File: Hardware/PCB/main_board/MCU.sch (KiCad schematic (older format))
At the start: 2 parts, among them J1 SWD, U2 NUCLEO-F446RE

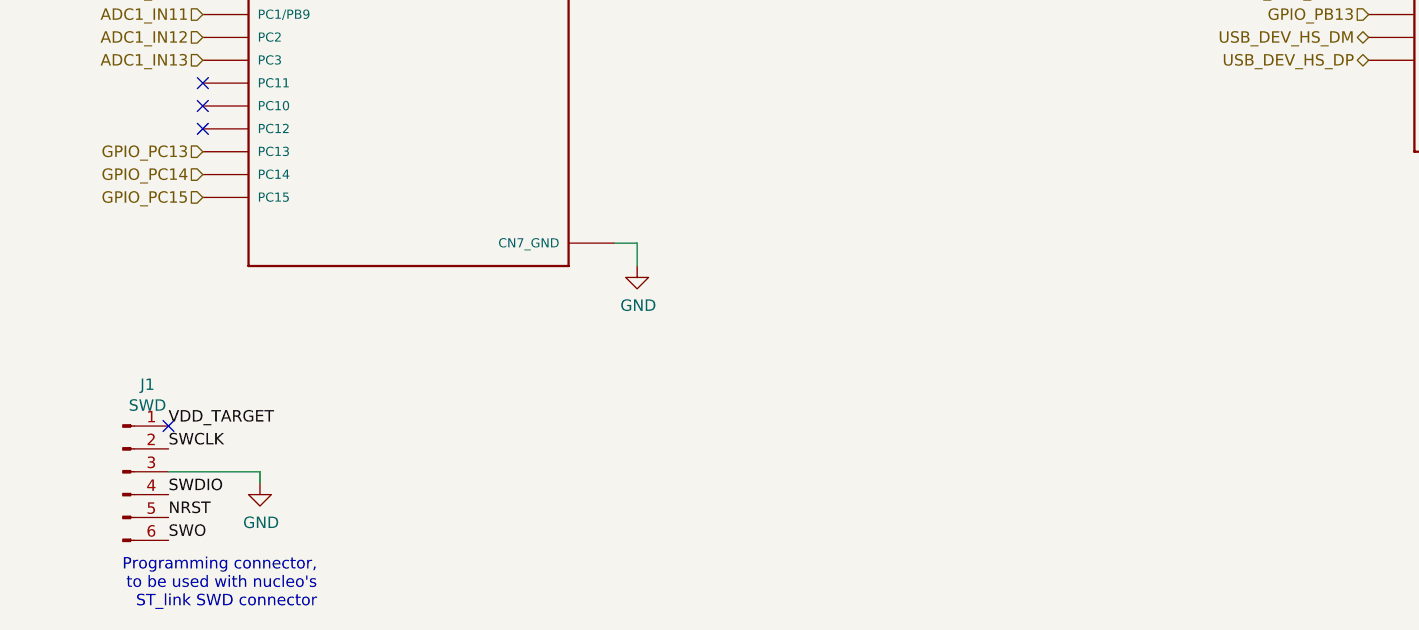
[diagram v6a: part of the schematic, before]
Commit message: Add test points headers
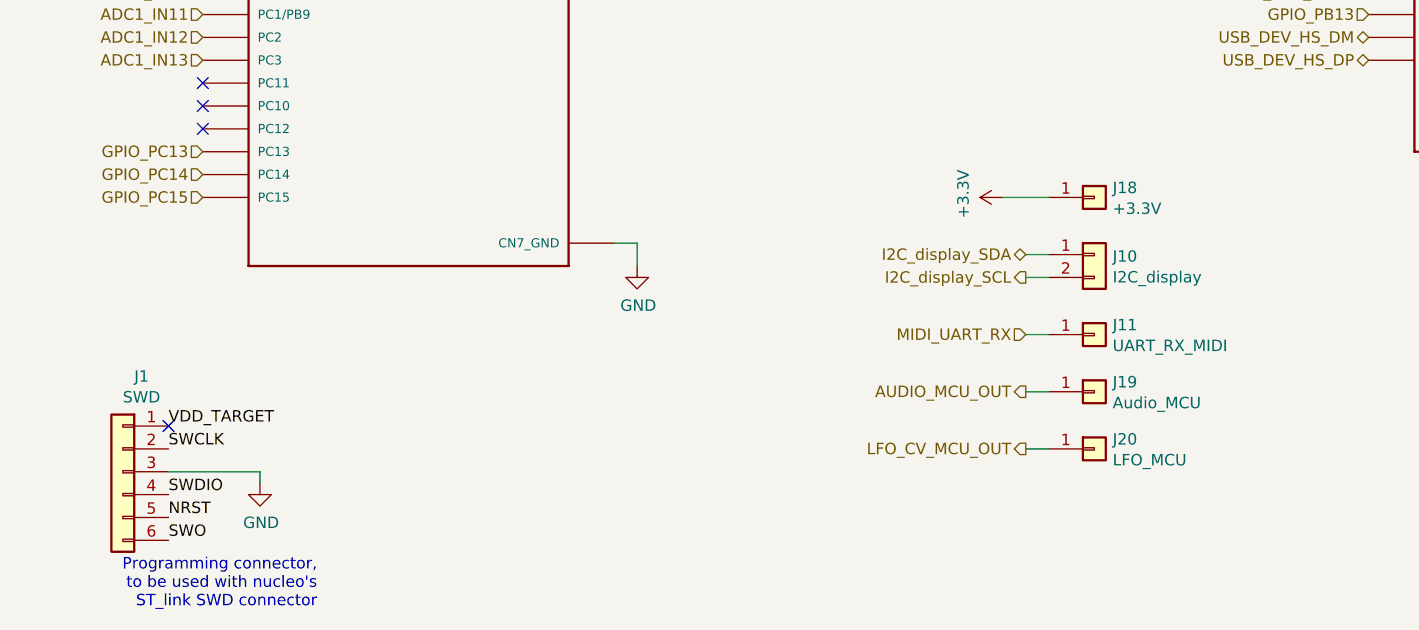
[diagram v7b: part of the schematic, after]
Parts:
- removed J1: SWD, Connector_PinHeader_2.54mm:PinHeader_1x06_P2.54mm_Vertical, symbol Connector:Conn_01x06_Male
- added J1: SWD, Connector_PinHeader_2.54mm:PinHeader_1x06_P2.54mm_Vertical, symbol Connector_Generic:Conn_01x06
- added J10: I2C_display, Connector_PinHeader_2.54mm:PinHeader_1x02_P2.54mm_Vertical, symbol Connector_Generic:Conn_01x02
- added J11: UART_RX_MIDI, Connector_PinHeader_2.54mm:PinHeader_1x01_P2.54mm_Vertical, symbol Connector_Generic:Conn_01x01
- added J18: +3.3V, Connector_PinHeader_2.54mm:PinHeader_1x01_P2.54mm_Vertical, symbol Connector_Generic:Conn_01x01
- added J19: Audio_MCU, Connector_PinHeader_2.54mm:PinHeader_1x01_P2.54mm_Vertical, symbol Connector_Generic:Conn_01x01
- added J20: LFO_MCU, Connector_PinHeader_2.54mm:PinHeader_1x01_P2.54mm_Vertical, symbol Connector_Generic:Conn_01x01
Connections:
- net +3V3: now also J18.1 (Pin_1)
- net AUDIO_MCU_OUT: now also J19.1 (Pin_1)
- net GND: now also J1.3 (Pin_3)
- net I2C_display_SCL: now also J10.2 (Pin_2)
- net I2C_display_SDA: now also J10.1 (Pin_1)
- net LFO_CV_MCU_OUT: now also J20.1 (Pin_1)
- net MIDI_UART_RX: now also J11.1 (Pin_1)
- net NRST: now also J1.5 (Pin_5)
- net SWCLK: now also J1.2 (Pin_2)
- net SWDIO: now also J1.4 (Pin_4)
- net SWO: now also J1.6 (Pin_6)
- net VDD_TARGET: now also J1.1 (Pin_1)
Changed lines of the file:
@@
 Text HLabel 7650 2250 0    50   Output ~ 0
 LFO_CV_MCU_OUT
-$Comp
-L Connector:Conn_01x06_Male J1
-U 1 1 5E51B937
-P 2200 6150
-F 0 "J1" H 2308 6531 50  0000 C CNN
-F 1 "SWD" H 2308 6440 50  0000 C CNN
-F 2 "Connector_PinHeader_2.54mm:PinHeader_1x06_P2.54mm_Vertical" H 2200 6150 50  0001 C CNN
-F 3 "~" H 2200 6150 50  0001 C CNN
-	1    2200 6150
-	1    0    0    -1
-$EndComp
 Text Label 2400 5950 0    50   ~ 0
 VDD_TARGET
@@
 USB_DEV_HS_DP
 NoConn ~ 2400 5950
+$Comp
+L Connector_Generic:Conn_01x02 J10
+U 1 1 5E7E23EF
+P 6450 5200
+F 0 "J10" H 6530 5192 50  0000 L CNN
+F 1 "I2C_display" H 6530 5101 50  0000 L CNN
+F 2 "Connector_PinHeader_2.54mm:PinHeader_1x02_P2.54mm_Vertical" H 6450 5200 50  0001 C CNN
+F 3 "~" H 6450 5200 50  0001 C CNN
+	1    6450 5200
+	1    0    0    -1
+$EndComp
+$Comp
+L Connector_Generic:Conn_01x06 J1
+U 1 1 5E7DA99C
+P 2200 6150
+F 0 "J1" H 2118 6567 50  0000 C CNN
+F 1 "SWD" H 2118 6476 50  0000 C CNN
+F 2 "Connector_PinHeader_2.54mm:PinHeader_1x06_P2.54mm_Vertical" H 2200 6150 50  0001 C CNN
+F 3 "~" H 2200 6150 50  0001 C CNN
+	1    2200 6150
+	-1   0    0    -1
+$EndComp
+Wire Wire Line
+	6150 5200 6250 5200
+Wire Wire Line
+	6150 5300 6250 5300
+Wire Wire Line
+	6150 5550 6250 5550
+Wire Wire Line
+	6150 5800 6250 5800
+Wire Wire Line
+	6150 6050 6250 6050
+$Comp
+L power:+3.3V #PWR0129
+U 1 1 5E80C3D2
+P 6050 4950
+F 0 "#PWR0129" H 6050 4800 50  0001 C CNN
+F 1 "+3.3V" H 6065 5123 50  0000 C CNN
+F 2 "" H 6050 4950 50  0001 C CNN
+F 3 "" H 6050 4950 50  0001 C CNN
+	1    6050 4950
+	0    -1   -1   0
+$EndComp
+Wire Wire Line
+	6050 4950 6250 4950
+Text HLabel 6150 6050 0    50   Output ~ 0
+LFO_CV_MCU_OUT
+Text HLabel 6150 5800 0    50   Output ~ 0
+AUDIO_MCU_OUT
+Text HLabel 6150 5550 0    50   Input ~ 0
+MIDI_UART_RX
+Text HLabel 6150 5300 0    50   Output ~ 0
+I2C_display_SCL
+Text HLabel 6150 5200 0    50   BiDi ~ 0
+I2C_display_SDA
+$Comp
+L Connector_Generic:Conn_01x01 J?
+U 1 1 5E8C724C
+P 6450 5800
+AR Path="/5E57C92D/5E8C724C" Ref="J?"  Part="1"
+AR Path="/5E658709/5E8C724C" Ref="J19"  Part="1"
+F 0 "J19" H 6530 5842 50  0000 L CNN
+F 1 "Audio_MCU" H 6530 5751 50  0000 L CNN
+F 2 "Connector_PinHeader_2.54mm:PinHeader_1x01_P2.54mm_Vertical" H 6450 5800 50  0001 C CNN
+F 3 "~" H 6450 5800 50  0001 C CNN
+	1    6450 5800
+	1    0    0    -1
+$EndComp
+$Comp
+L Connector_Generic:Conn_01x01 J?
+U 1 1 5E8CCEE2
+P 6450 6050
+AR Path="/5E57C92D/5E8CCEE2" Ref="J?"  Part="1"
+AR Path="/5E658709/5E8CCEE2" Ref="J20"  Part="1"
+F 0 "J20" H 6530 6092 50  0000 L CNN
+F 1 "LFO_MCU" H 6530 6001 50  0000 L CNN
+F 2 "Connector_PinHeader_2.54mm:PinHeader_1x01_P2.54mm_Vertical" H 6450 6050 50  0001 C CNN
+F 3 "~" H 6450 6050 50  0001 C CNN
+	1    6450 6050
+	1    0    0    -1
+$EndComp
+$Comp
+L Connector_Generic:Conn_01x01 J?
+U 1 1 5E8CFEC0
+P 6450 4950
+AR Path="/5E57C92D/5E8CFEC0" Ref="J?"  Part="1"
+AR Path="/5E658709/5E8CFEC0" Ref="J18"  Part="1"
+F 0 "J18" H 6530 4992 50  0000 L CNN
+F 1 "+3.3V" H 6530 4901 50  0000 L CNN
+F 2 "Connector_PinHeader_2.54mm:PinHeader_1x01_P2.54mm_Vertical" H 6450 4950 50  0001 C CNN
+F 3 "~" H 6450 4950 50  0001 C CNN
+	1    6450 4950
+	1    0    0    -1
+$EndComp
+$Comp
+L Connector_Generic:Conn_01x01 J?
+U 1 1 5E90C91E
+P 6450 5550
+AR Path="/5E57C92D/5E90C91E" Ref="J?"  Part="1"
+AR Path="/5E658709/5E90C91E" Ref="J11"  Part="1"
+F 0 "J11" H 6530 5592 50  0000 L CNN
+F 1 "UART_RX_MIDI" H 6530 5501 50  0000 L CNN
+F 2 "Connector_PinHeader_2.54mm:PinHeader_1x01_P2.54mm_Vertical" H 6450 5550 50  0001 C CNN
+F 3 "~" H 6450 5550 50  0001 C CNN
+	1    6450 5550
+	1    0    0    -1
+$EndComp
 $EndSCHEMATC

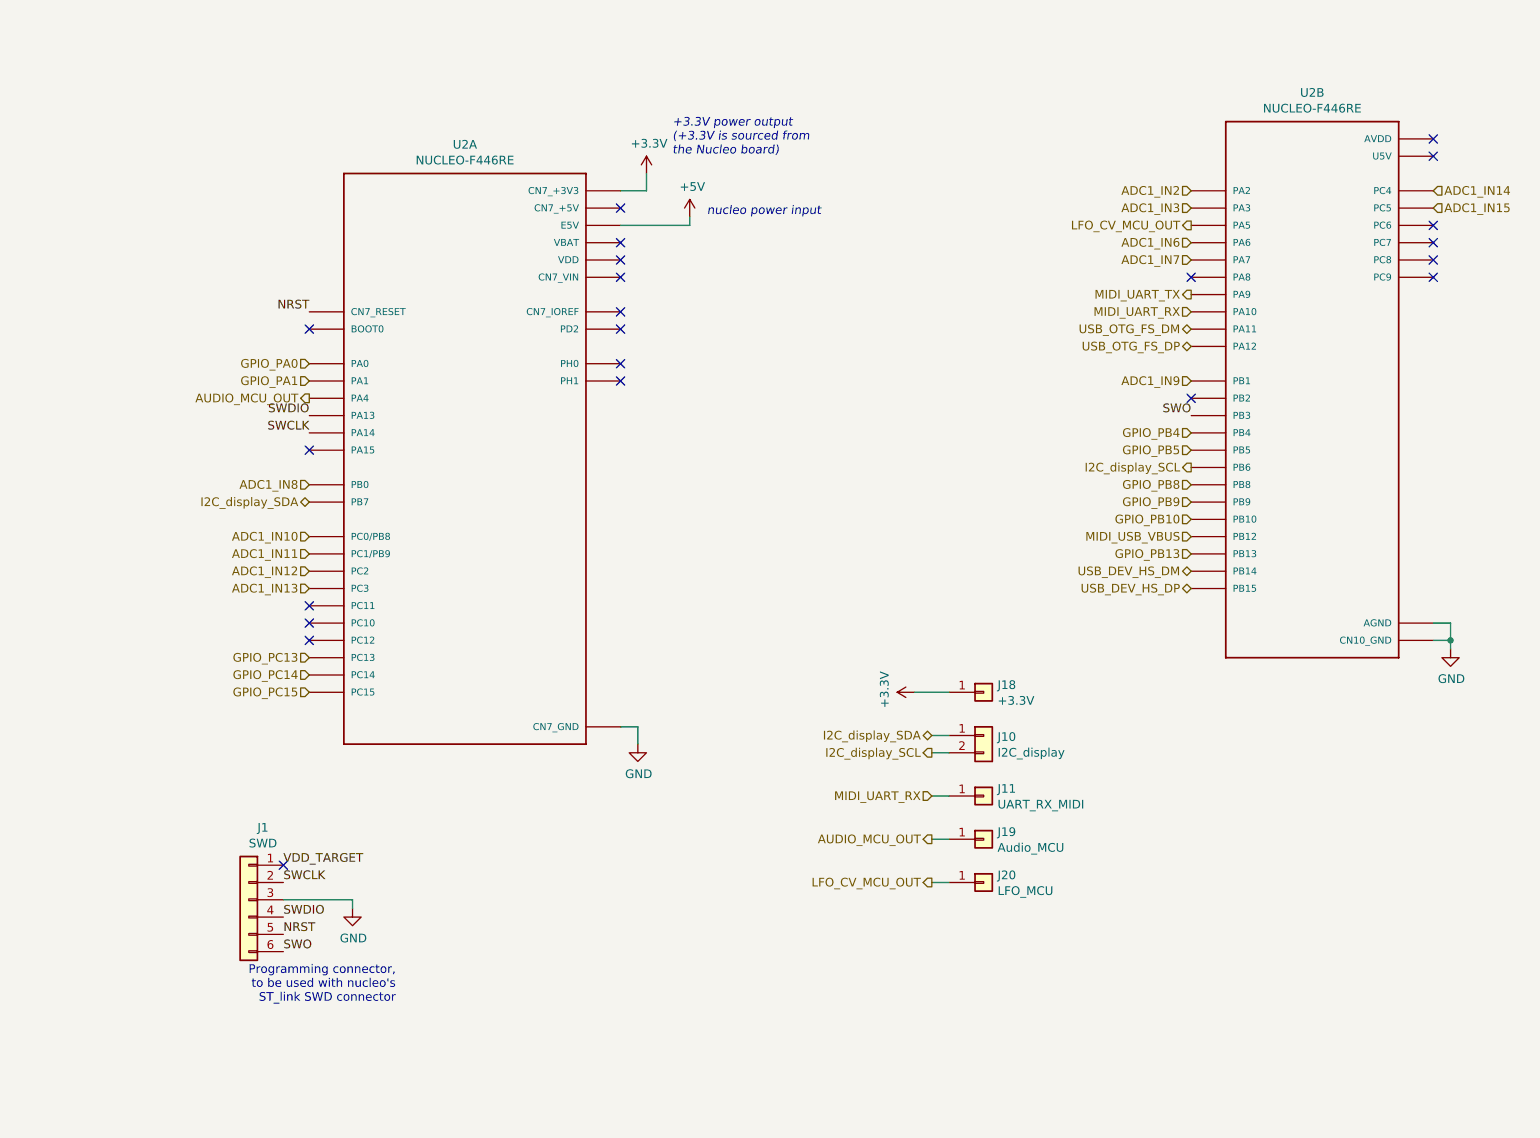
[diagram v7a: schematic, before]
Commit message: Use bare STM32 instead of nucleo board. Schematics update
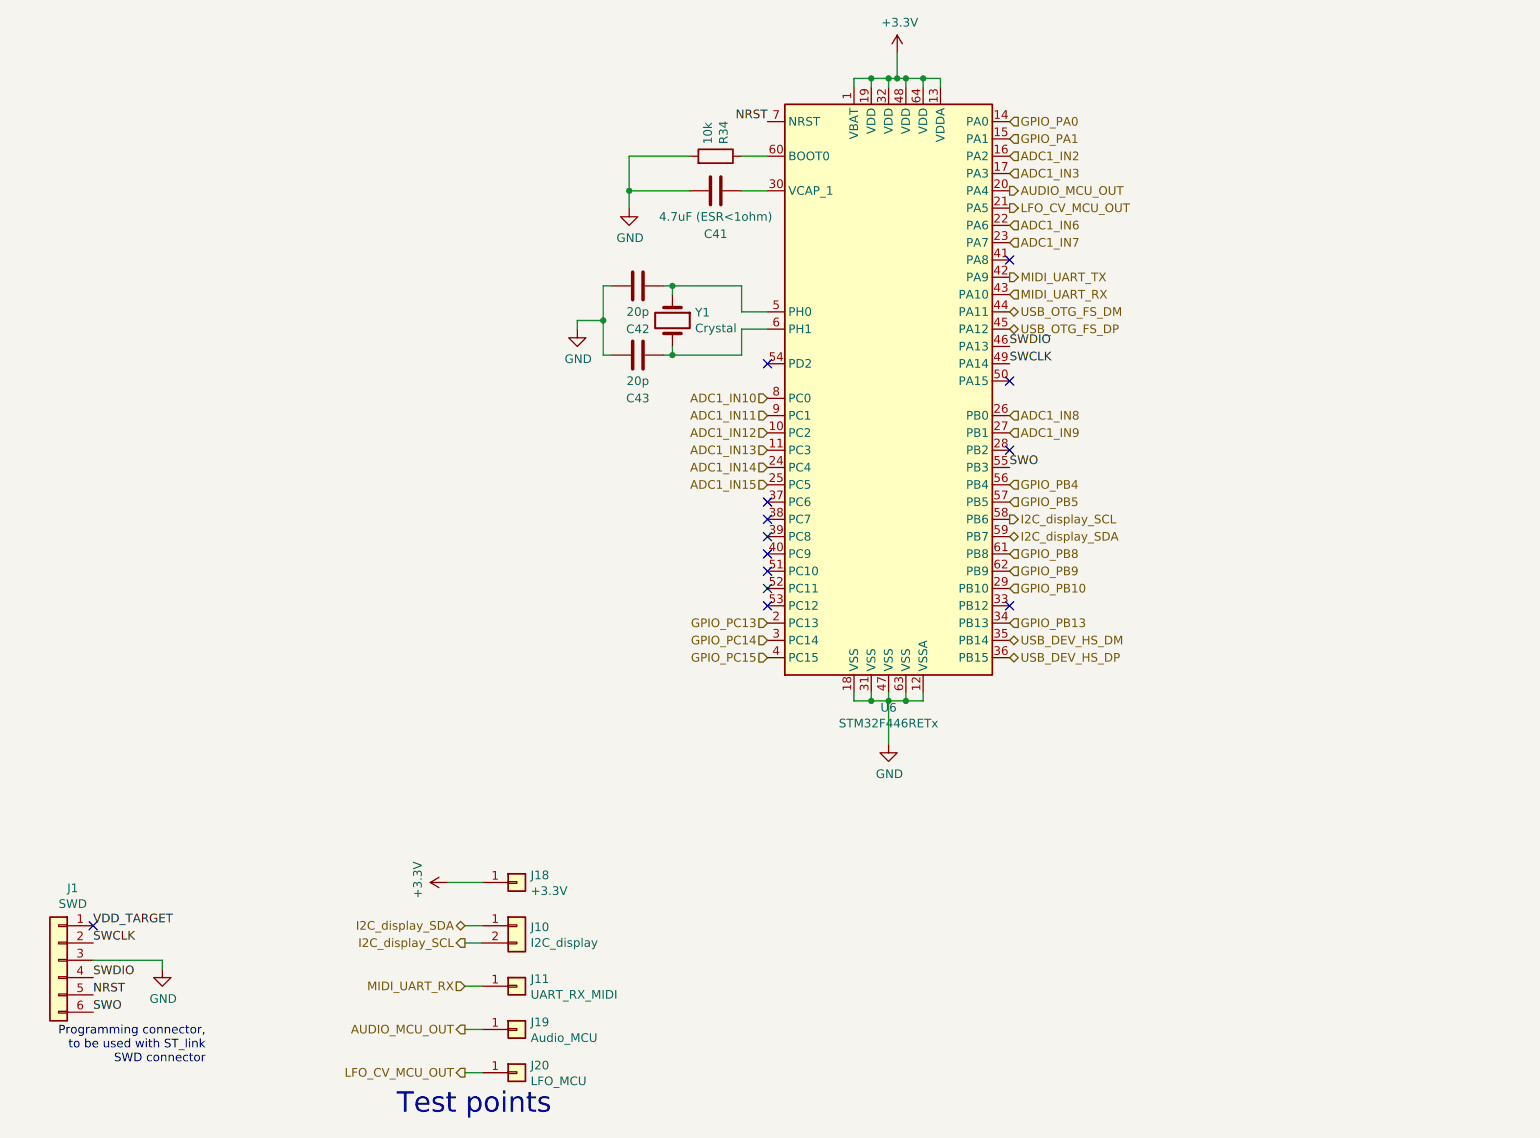
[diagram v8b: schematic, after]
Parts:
- removed U2: NUCLEO-F446RE, lib:MODULE_NUCLEO-F446RE, symbol NUCLEO-F446RE:NUCLEO-F446RE
- added C41: 4.7uF (ESR<1ohm), Capacitor_SMD:C_0805_2012Metric, symbol Device:C
- added C42, C43: 20p, Capacitor_SMD:C_0805_2012Metric, symbol Device:C
- added R34: 10k, Resistor_SMD:R_0805_2012Metric, symbol Device:R
- added U6: STM32F446RETx, Package_QFP:LQFP-64_10x10mm_P0.5mm, symbol MCU_ST_STM32F4:STM32F446RETx
- added Y1: Crystal, Crystal:Crystal_SMD_3225-4Pin_3.2x2.5mm_HandSoldering, symbol Device:Crystal
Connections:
- net +3V3: now also U6.1 (VBAT), U6.13 (VDDA), U6.19 (VDD), U6.32 (VDD), U6.48 (VDD), U6.64 (VDD)
- net ADC1_IN10: now also U6.8 (PC0)
- net ADC1_IN11: now also U6.9 (PC1)
- net ADC1_IN12: now also U6.10 (PC2)
- net ADC1_IN13: now also U6.11 (PC3)
- net ADC1_IN14: now also U6.24 (PC4)
- net ADC1_IN15: now also U6.25 (PC5)
- net ADC1_IN2: now also U6.16 (PA2)
- net ADC1_IN3: now also U6.17 (PA3)
- net ADC1_IN6: now also U6.22 (PA6)
- net ADC1_IN7: now also U6.23 (PA7)
- net ADC1_IN8: now also U6.26 (PB0)
- net ADC1_IN9: now also U6.27 (PB1)
- net AUDIO_MCU_OUT: now also U6.20 (PA4)
- net GND: now also C41.1, C42.1, C43.1, R34.2, U6.12 (VSSA), U6.18 (VSS), U6.31 (VSS), U6.47 (VSS), U6.63 (VSS)
- net GPIO_PA0: now also U6.14 (PA0)
- net GPIO_PA1: now also U6.15 (PA1)
- net GPIO_PB10: now also U6.29 (PB10)
- net GPIO_PB13: now also U6.34 (PB13)
- net GPIO_PB4: now also U6.56 (PB4)
- net GPIO_PB5: now also U6.57 (PB5)
- net GPIO_PB8: now also U6.61 (PB8)
- net GPIO_PB9: now also U6.62 (PB9)
- net GPIO_PC13: now also U6.2 (PC13)
- net GPIO_PC14: now also U6.3 (PC14)
- net GPIO_PC15: now also U6.4 (PC15)
- net I2C_display_SCL: now also U6.58 (PB6)
- net I2C_display_SDA: now also U6.59 (PB7)
- net LFO_CV_MCU_OUT: now also U6.21 (PA5)
- net MIDI_UART_RX: now also U6.43 (PA10)
- net MIDI_UART_TX: now also U6.42 (PA9)
- net NRST: now also U6.7 (NRST)
- net SWCLK: now also U6.49 (PA14)
- net SWDIO: now also U6.46 (PA13)
- net SWO: now also U6.55 (PB3)
- net USB_DEV_HS_DM: now also U6.35 (PB14)
- net USB_DEV_HS_DP: now also U6.36 (PB15)
- net USB_OTG_FS_DM: now also U6.44 (PA11)
- net USB_OTG_FS_DP: now also U6.45 (PA12)
- new net: C41.2, U6.30 (VCAP_1)
- new net: C42.2, U6.5 (PH0), Y1.1
- new net: C43.2, U6.6 (PH1), Y1.2
- new net: R34.1, U6.60 (BOOT0)
- no-connect marks 22 -> 13
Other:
- note added: "Programming connector,\nto be used with ST_link \nSWD connector"
- note added: "Test points"
- note removed: "+3.3V power output\n(+3.3V is sourced from\nthe Nucleo board)"
- note removed: "Programming connector,\nto be used with nucleo's\nST_link SWD connector"
- note removed: "nucleo power input"
- moved on the sheet: J1, J10, J11, J18, J19, J20
